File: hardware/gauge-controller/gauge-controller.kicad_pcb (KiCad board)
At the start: 4 copper layers, 50 x 50 mm, 98 parts, among them J1 USB4120-03-C_REVA, J2 PWR_CAN, J4 Conn_01x12, Q1 Q_NPN_EBC, SW1 SW_Push, SW2 SW_Push, U1 ESP32-S3R2, U2 SN65HVD230, U3 W25Q128JVS, U5 ADP2303ARDZ-3.3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

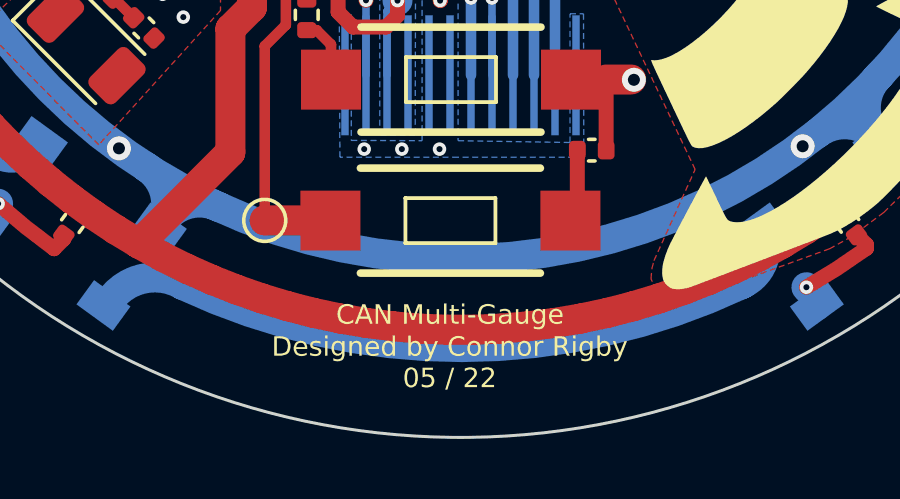
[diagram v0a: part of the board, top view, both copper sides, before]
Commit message: Update images and project names
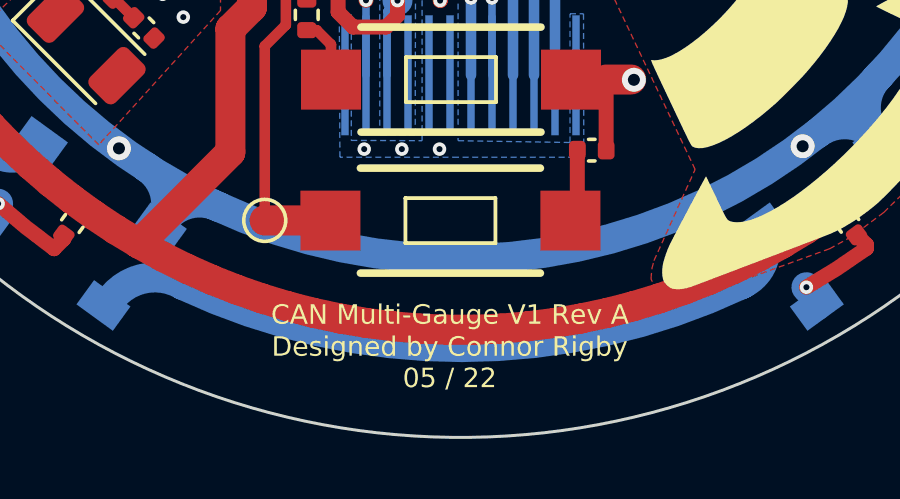
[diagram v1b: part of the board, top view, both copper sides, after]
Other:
- board text added: "CAN Multi-Gauge V1 Rev A"
- board text removed: "CAN Multi-Gauge"
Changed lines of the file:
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@@
   (gr_arc (start 56.67 22.869999) (mid 55.88745 23.360397) (end 54.976172 23.210578) (layer "User.8") (width 0.15))
   (gr_arc (start 65.11 45.65) (mid 65.777025 44.727938) (end 66.901659 44.553813) (layer "User.8") (width 0.15))
-  (gr_arc (start 64.620002 33.8) (mid 64.625001 32.767724) (end 65.349707 32.03259) (layer "User.8") (width 0.15))
+  (gr_arc (start 64.620002 33.8) (mid 64.625001 32.767723) (end 65.349707 32.03259) (layer "User.8") (width 0.15))
   (gr_arc (start 68.38063 31.047469) (mid 67.036789 31.054871) (end 66.098731 30.092578) (layer "User.8") (width 0.15))
   (gr_arc (start 66.81829 36.698084) (mid 67.929278 36.905864) (end 68.58 37.83) (layer "User.8") (width 0.15))
@@
     (effects (font (size 0.65 0.65) (thickness 0.15)))
   )
-  (gr_text "CAN Multi-Gauge" (at 46.39 61.49) (layer "F.SilkS")
+  (gr_text "CAN Multi-Gauge V1 Rev A" (at 46.39 61.49) (layer "F.SilkS")
     (effects (font (size 0.65 0.65) (thickness 0.15)))
   )
